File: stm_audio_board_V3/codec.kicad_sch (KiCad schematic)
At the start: 12 parts

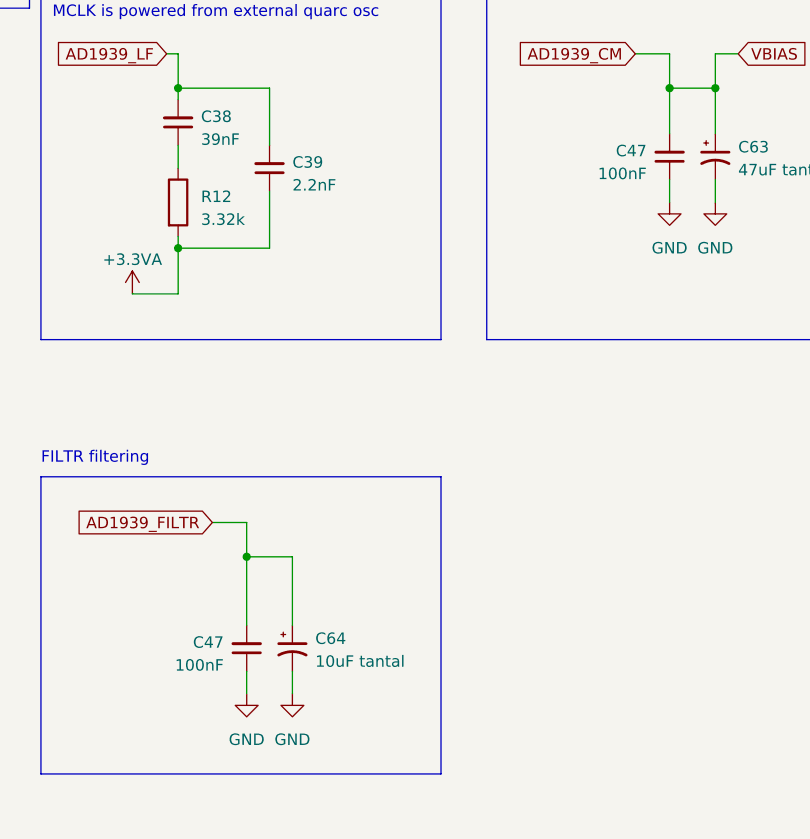
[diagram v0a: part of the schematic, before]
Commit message: Input and output stages are made and assembly started on pcb view
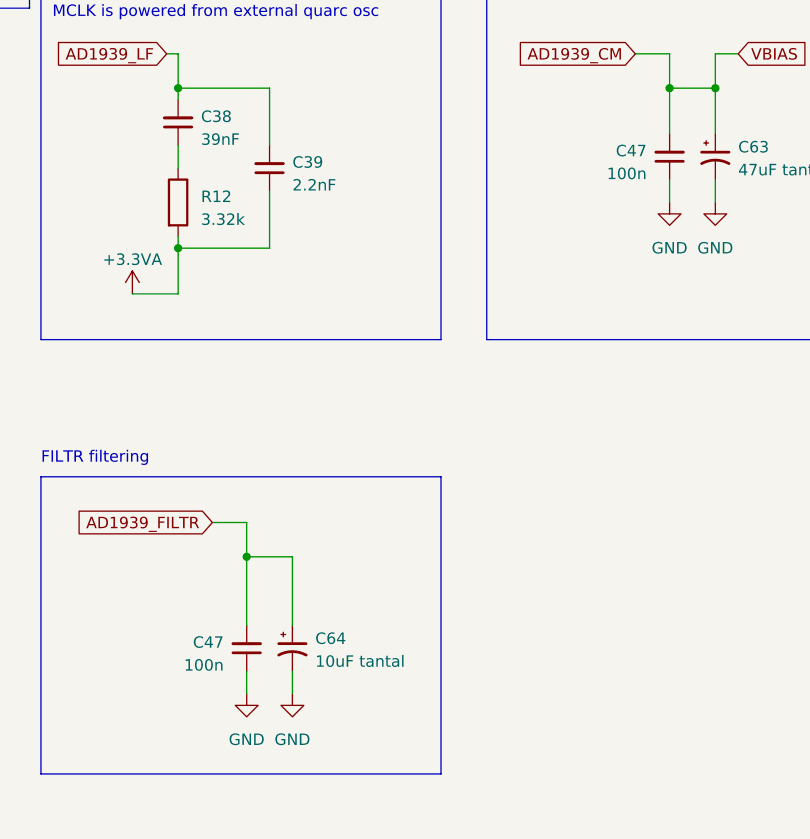
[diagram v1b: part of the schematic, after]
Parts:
- C39: footprint Capacitor_SMD:C_0603_1608Metric_Pad1.08x0.95mm_HandSolder -> Capacitor_SMD:C_0603_1608Metric
- C47: value 100nF -> 100n; footprint Capacitor_SMD:C_0603_1608Metric_Pad1.08x0.95mm_HandSolder -> Capacitor_SMD:C_0603_1608Metric
- R12: footprint Resistor_SMD:R_0805_2012Metric_Pad1.20x1.40mm_HandSolder -> Resistor_SMD:R_0603_1608Metric
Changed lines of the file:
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@@
       (effects (font (size 1.27 1.27)) (justify left))
     )
-    (property "Footprint" "Resistor_SMD:R_0805_2012Metric_Pad1.20x1.40mm_HandSolder" (at 150.622 53.34 90)
+    (property "Footprint" "Resistor_SMD:R_0603_1608Metric" (at 150.622 53.34 90)
       (effects (font (size 1.27 1.27)) hide)
     )
@@
       (effects (font (size 1.27 1.27)) (justify right))
     )
-    (property "Value" "100nF" (at 204.47 50.1586 0)
-      (effects (font (size 1.27 1.27)) (justify right))
-    )
-    (property "Footprint" "Capacitor_SMD:C_0603_1608Metric_Pad1.08x0.95mm_HandSolder" (at 207.01 48.26 0)
+    (property "Value" "100n" (at 204.47 50.1586 0)
+      (effects (font (size 1.27 1.27)) (justify right))
+    )
+    (property "Footprint" "Capacitor_SMD:C_0603_1608Metric" (at 207.01 48.26 0)
       (effects (font (size 1.27 1.27)) hide)
     )
@@
       (effects (font (size 1.27 1.27)) (justify right))
     )
-    (property "Footprint" "Capacitor_SMD:C_0603_1608Metric_Pad1.08x0.95mm_HandSolder" (at 162.56 49.53 0)
+    (property "Footprint" "Capacitor_SMD:C_0603_1608Metric" (at 162.56 49.53 0)
       (effects (font (size 1.27 1.27)) hide)
     )
@@
       (effects (font (size 1.27 1.27)) (justify right))
     )
-    (property "Value" "100nF" (at 157.48 104.7686 0)
-      (effects (font (size 1.27 1.27)) (justify right))
-    )
-    (property "Footprint" "Capacitor_SMD:C_0603_1608Metric_Pad1.08x0.95mm_HandSolder" (at 160.02 102.87 0)
-      (effects (font (size 1.27 1.27)) hide)
-    )
+    (property "Value" "100n" (at 157.48 104.7686 0)
+      (effects (font (size 1.27 1.27)) (justify right))
+    )
+    (property "Footprint" "Capacitor_SMD:C_0603_1608Metric" (at 160.02 102.87 0)
+      (effects (font (size 1.27 1.27)) hide)
+    )

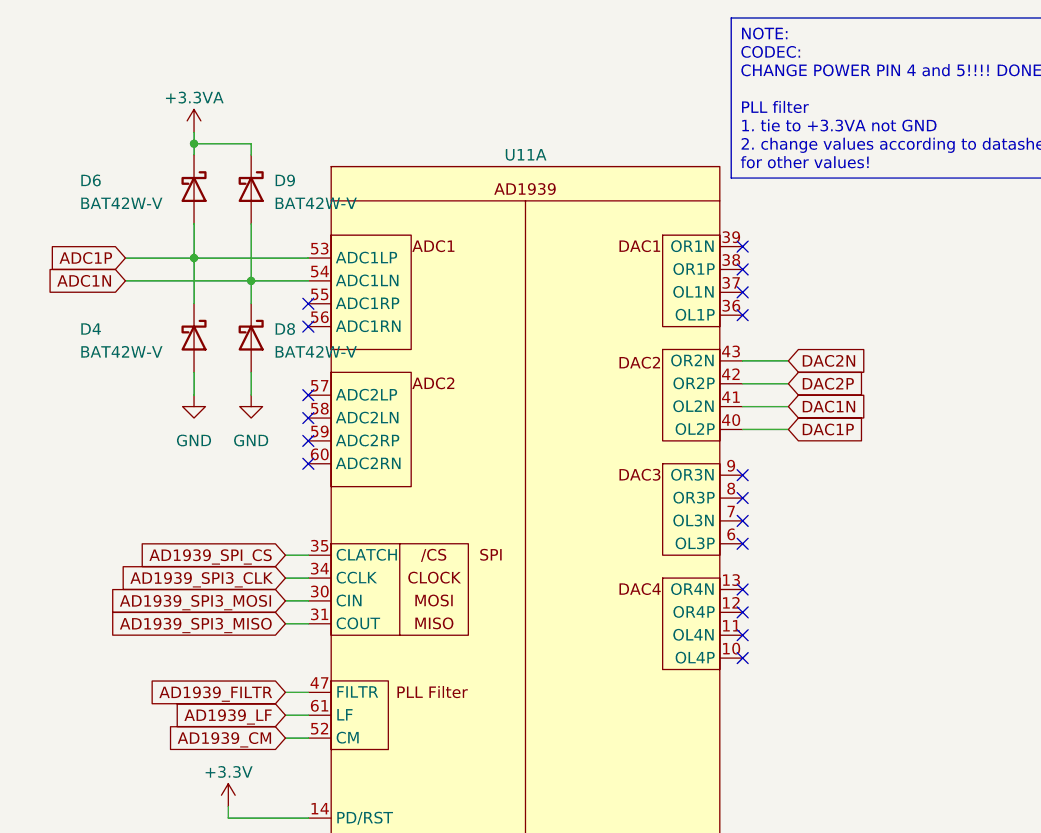
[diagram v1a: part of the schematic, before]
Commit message: Input output connected to codec
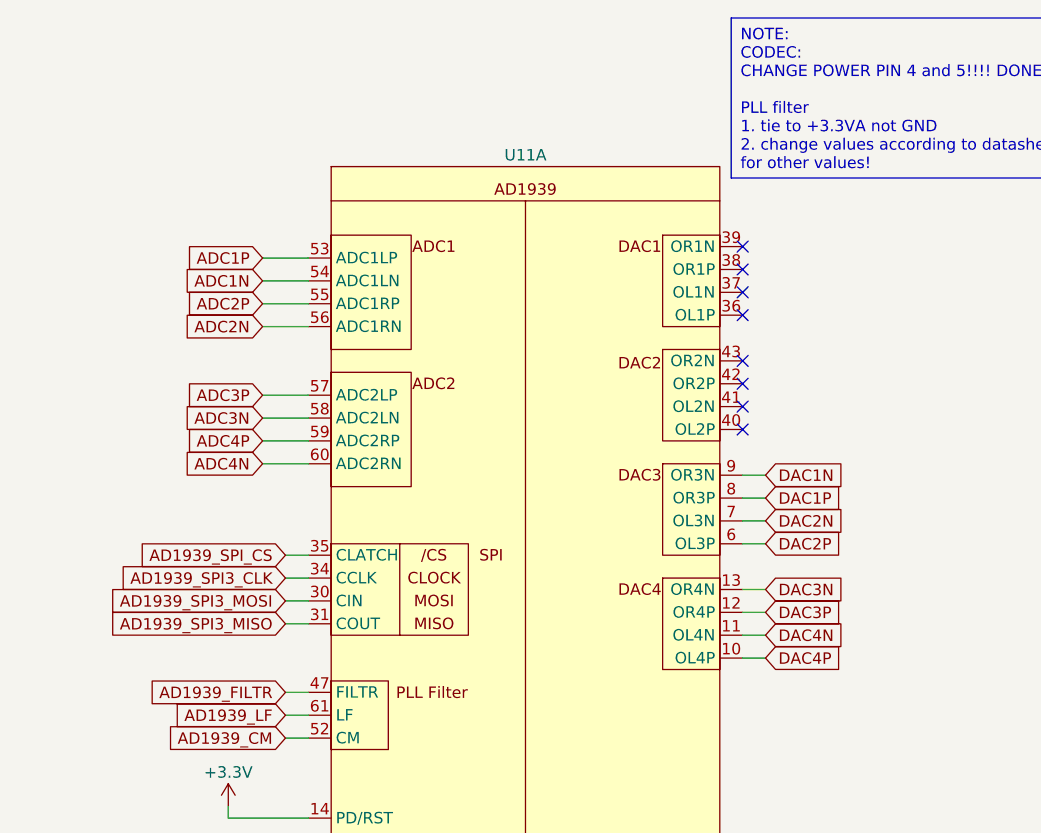
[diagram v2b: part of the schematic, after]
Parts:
- removed D4, D6, D8, D9: BAT42W-V, Diode_SMD:D_SOD-123, symbol Diode:BAT42W-V
- U11: JLCPCB (none) -> C2913556
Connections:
- net DAC1N: now also U11.9 (OR3N); no longer U11.41 (OL2N)
- net DAC1P: now also U11.8 (OR3P); no longer U11.40 (OL2P)
- net DAC2N: now also U11.7 (OL3N); no longer U11.43 (OR2N)
- net DAC2P: now also U11.6 (OL3P); no longer U11.42 (OR2P)
- net DAC4P: now reaches U11.10 (OL4P)
- net DAC4N: now reaches U11.11 (OL4N)
- net DAC3P: now reaches U11.12 (OR4P)
- net DAC3N: now reaches U11.13 (OR4N)
- net ADC2P: now reaches U11.55 (ADC1RP)
- net ADC2N: now reaches U11.56 (ADC1RN)
- net ADC3P: now reaches U11.57 (ADC2LP)
- net ADC3N: now reaches U11.58 (ADC2LN)
- net ADC4P: now reaches U11.59 (ADC2RP)
- net ADC4N: now reaches U11.60 (ADC2RN)
- no-connect marks 22 -> 12

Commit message: minor changes
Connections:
- net AD1939_I2S2_CK is gone; now on net AD1939_SAI1A_CK: U11.21 (DBCLK)
- net AD1939_I2S2_WS is gone; now on net AD1939_SAI1A_WS: U11.22 (DLRCLK)
- net AD1939_SAI1A_SDO: now reaches U11.20 (DSDATA1)
- net AD1939_I2S1_CK renamed AD1939_SAI1A_CK
- net AD1939_I2S1_SDI renamed AD1939_SAI1B_SDI
- net AD1939_I2S1_WS renamed AD1939_SAI1A_WS
- net AD1939_I2S2_SDO: no longer names the net of U11.19 (DSDATA2)
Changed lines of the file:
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@@
   (no_connect (at 92.71 54.61))
   (no_connect (at 92.71 44.45))
-  (no_connect (at 92.71 123.19))
   (no_connect (at 92.71 39.37))
   (no_connect (at 92.71 57.15))
+  (no_connect (at 92.71 120.65))
   (no_connect (at 44.45 118.11))
   (wire (pts (xy 95.25 82.55) (xy 92.71 82.55))
@@
     (stroke (width 0) (type default))
   )
-  (wire (pts (xy 92.71 120.65) (xy 97.79 120.65))
-    (stroke (width 0) (type default))
-  )
   (wire (pts (xy 152.4 58.42) (xy 152.4 63.5))
     (stroke (width 0) (type default))
@@
   )
   (wire (pts (xy 160.02 92.71) (xy 160.02 100.33))
+    (stroke (width 0) (type default))
+  )
+  (wire (pts (xy 92.71 123.19) (xy 97.79 123.19))
     (stroke (width 0) (type default))
   )
@@
     (effects (font (size 1.27 1.27)) (justify left bottom))
   )
-  (global_label "AD1939_I2S1_SDI" (shape input) (at 34.29 115.57 180) (fields_autoplaced)
-    (effects (font (size 1.27 1.27)) (justify right))
-    (property "Intersheetrefs" "${INTERSHEET_REFS}" (at 14.9348 115.57 0)
-      (effects (font (size 1.27 1.27)) (justify right) hide)
-    )
-  )
-  (global_label "AD1939_I2S2_SDO" (shape input) (at 97.79 120.65 0) (fields_autoplaced)
-    (effects (font (size 1.27 1.27)) (justify left))
-    (property "Intersheetrefs" "${INTERSHEET_REFS}" (at 117.8709 120.65 0)
+  (global_label "AD1939_SAI1B_SDI" (shape input) (at 34.29 115.57 180) (fields_autoplaced)
+    (effects (font (size 1.27 1.27)) (justify right))
+    (property "Intersheetrefs" "${INTERSHEET_REFS}" (at 13.7857 115.57 0)
+      (effects (font (size 1.27 1.27)) (justify right) hide)
+    )
+  )
+  (global_label "AD1939_SAI1A_SDO" (shape input) (at 97.79 123.19 0) (fields_autoplaced)
+    (effects (font (size 1.27 1.27)) (justify left))
+    (property "Intersheetrefs" "${INTERSHEET_REFS}" (at 118.8386 123.19 0)
+      (effects (font (size 1.27 1.27)) (justify left) hide)
+    )
+  )
+  (global_label "AD1939_SAI1A_CK" (shape input) (at 97.79 111.76 0) (fields_autoplaced)
+    (effects (font (size 1.27 1.27)) (justify left))
+    (property "Intersheetrefs" "${INTERSHEET_REFS}" (at 117.5686 111.76 0)
       (effects (font (size 1.27 1.27)) (justify left) hide)
     )
@@
     )
   )
+  (global_label "AD1939_SAI1A_WS" (shape input) (at 97.79 109.22 0) (fields_autoplaced)
+    (effects (font (size 1.27 1.27)) (justify left))
+    (property "Intersheetrefs" "${INTERSHEET_REFS}" (at 117.6895 109.22 0)
+      (effects (font (size 1.27 1.27)) (justify left) hide)
+    )
+  )
   (global_label "AD1939_FILTR" (shape input) (at 41.91 88.9 180) (fields_autoplaced)
     (effects (font (size 1.27 1.27)) (justify right))
@@
     )
   )
-  (global_label "AD1939_I2S1_CK" (shape input) (at 34.29 111.76 180) (fields_autoplaced)
-    (effects (font (size 1.27 1.27)) (justify right))
-    (property "Intersheetrefs" "${INTERSHEET_REFS}" (at 15.4791 111.76 0)
-      (effects (font (size 1.27 1.27)) (justify right) hide)
-    )
-  )
-  (global_label "AD1939_I2S2_CK" (shape input) (at 97.79 111.76 0) (fields_autoplaced)
-    (effects (font (size 1.27 1.27)) (justify left))
-    (property "Intersheetrefs" "${INTERSHEET_REFS}" (at 116.6009 111.76 0)
-      (effects (font (size 1.27 1.27)) (justify left) hide)
+  (global_label "AD1939_SAI1A_CK" (shape input) (at 34.29 111.76 180) (fields_autoplaced)
+    (effects (font (size 1.27 1.27)) (justify right))
+    (property "Intersheetrefs" "${INTERSHEET_REFS}" (at 14.5114 111.76 0)
+      (effects (font (size 1.27 1.27)) (justify right) hide)
     )
   )
@@
     )
   )
-  (global_label "AD1939_I2S1_WS" (shape input) (at 34.29 109.22 180) (fields_autoplaced)
-    (effects (font (size 1.27 1.27)) (justify right))
-    (property "Intersheetrefs" "${INTERSHEET_REFS}" (at 15.3582 109.22 0)
+  (global_label "AD1939_SAI1A_WS" (shape input) (at 34.29 109.22 180) (fields_autoplaced)
+    (effects (font (size 1.27 1.27)) (justify right))
+    (property "Intersheetrefs" "${INTERSHEET_REFS}" (at 14.3905 109.22 0)
       (effects (font (size 1.27 1.27)) (justify right) hide)
     )
@@
     )
   )
-  (global_label "AD1939_I2S2_WS" (shape input) (at 97.79 109.22 0) (fields_autoplaced)
-    (effects (font (size 1.27 1.27)) (justify left))
-    (property "Intersheetrefs" "${INTERSHEET_REFS}" (at 116.7218 109.22 0)
-      (effects (font (size 1.27 1.27)) (justify left) hide)
-    )
-  )

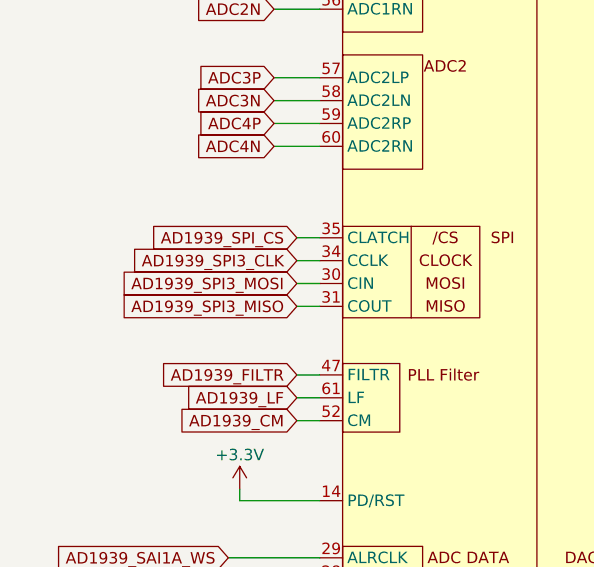
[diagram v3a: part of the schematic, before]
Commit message: Reworked outline for enclosure
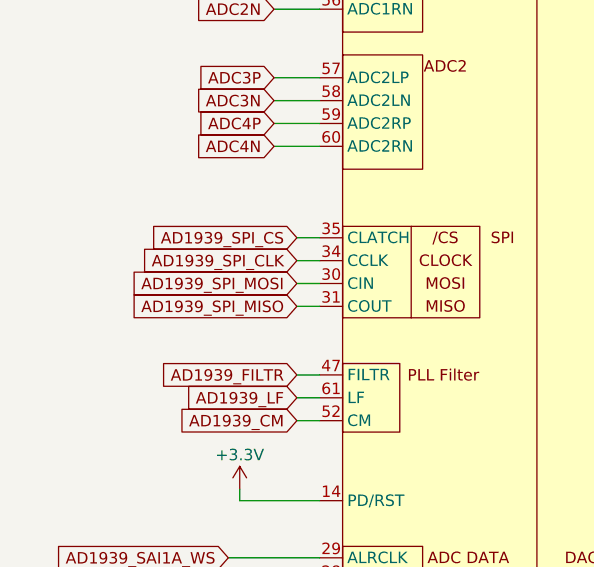
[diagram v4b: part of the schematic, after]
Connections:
- net AD1939_SPI3_CLK renamed AD1939_SPI_CLK
- net AD1939_SPI3_MISO renamed AD1939_SPI_MISO
- net AD1939_SPI3_MOSI renamed AD1939_SPI_MOSI
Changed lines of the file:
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@@
     )
   )
-  (global_label "AD1939_SPI3_MISO" (shape input) (at 41.91 81.28 180) (fields_autoplaced)
+  (global_label "AD1939_SPI_MISO" (shape input) (at 41.91 81.28 180) (fields_autoplaced)
     (effects (font (size 1.27 1.27)) (justify right))
-    (property "Intersheetrefs" "${INTERSHEET_REFS}" (at 20.9824 81.28 0)
+    (property "Intersheetrefs" "${INTERSHEET_REFS}" (at 22.1919 81.28 0)
       (effects (font (size 1.27 1.27)) (justify right) hide)
     )
@@
     )
   )
-  (global_label "AD1939_SPI3_MOSI" (shape input) (at 41.91 78.74 180) (fields_autoplaced)
+  (global_label "AD1939_SPI_MOSI" (shape input) (at 41.91 78.74 180) (fields_autoplaced)
     (effects (font (size 1.27 1.27)) (justify right))
-    (property "Intersheetrefs" "${INTERSHEET_REFS}" (at 20.9824 78.74 0)
+    (property "Intersheetrefs" "${INTERSHEET_REFS}" (at 22.1919 78.74 0)
       (effects (font (size 1.27 1.27)) (justify right) hide)
     )
@@
     )
   )
-  (global_label "AD1939_SPI3_CLK" (shape input) (at 41.91 76.2 180) (fields_autoplaced)
+  (global_label "AD1939_SPI_CLK" (shape input) (at 41.91 76.2 180) (fields_autoplaced)
     (effects (font (size 1.27 1.27)) (justify right))
-    (property "Intersheetrefs" "${INTERSHEET_REFS}" (at 22.0105 76.2 0)
+    (property "Intersheetrefs" "${INTERSHEET_REFS}" (at 23.22 76.2 0)
       (effects (font (size 1.27 1.27)) (justify right) hide)
     )

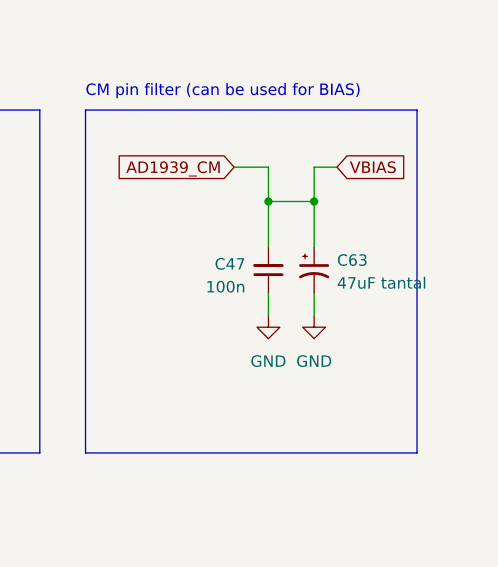
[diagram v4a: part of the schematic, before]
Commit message: gnd vias added, footswitch mux connected
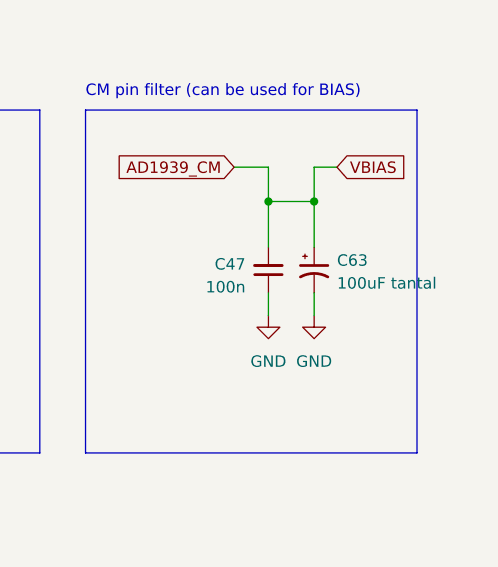
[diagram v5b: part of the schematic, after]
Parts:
- C63: value 47uF tantal -> 100uF tantal; footprint Capacitor_Tantalum_SMD:CP_EIA-7343-31_Kemet-D_Pad2.25x2.55mm_HandSolder -> Capacitor_Tantalum_SMD:CP_EIA-3528-21_Kemet-B; JLCPCB (none) -> C16133
- C64: footprint Capacitor_Tantalum_SMD:CP_EIA-6032-28_Kemet-C_Pad2.25x2.35mm_HandSolder -> Capacitor_Tantalum_SMD:CP_EIA-3216-18_Kemet-A; JLCPCB (none) -> C7171
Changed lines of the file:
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@@
       (effects (font (size 1.27 1.27)) (justify left))
     )
-    (property "Footprint" "Capacitor_Tantalum_SMD:CP_EIA-6032-28_Kemet-C_Pad2.25x2.35mm_HandSolder" (at 165.1 102.87 0)
+    (property "Footprint" "Capacitor_Tantalum_SMD:CP_EIA-3216-18_Kemet-A" (at 165.1 102.87 0)
       (effects (font (size 1.27 1.27)) hide)
     )
     (property "Datasheet" "~" (at 165.1 102.87 0)
+      (effects (font (size 1.27 1.27)) hide)
+    )
+    (property "JLCPCB" "C7171" (at 165.1 102.87 0)
       (effects (font (size 1.27 1.27)) hide)
     )
@@
       (effects (font (size 1.27 1.27)) (justify left))
     )
-    (property "Value" "47uF tantal" (at 214.63 49.7332 0)
+    (property "Value" "100uF tantal" (at 214.63 49.7332 0)
       (effects (font (size 1.27 1.27)) (justify left))
     )
-    (property "Footprint" "Capacitor_Tantalum_SMD:CP_EIA-7343-31_Kemet-D_Pad2.25x2.55mm_HandSolder" (at 212.09 48.26 0)
+    (property "Footprint" "Capacitor_Tantalum_SMD:CP_EIA-3528-21_Kemet-B" (at 212.09 48.26 0)
       (effects (font (size 1.27 1.27)) hide)
     )
@@
       (effects (font (size 1.27 1.27)) hide)
     )
+    (property "JLCPCB" "C16133" (at 212.09 48.26 0)
+      (effects (font (size 1.27 1.27)) hide)
+    )
